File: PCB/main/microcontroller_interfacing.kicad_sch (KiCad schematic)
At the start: 11 parts, among them U1 USB_Micro_B_Female_Connector, U2 CH340G, U3 AT24C256C-SSHL-T, X1 12MHz_SMD_Crystal

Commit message: Update Schematic and BOM
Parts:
- C1, C2: Extended/Basic (none) -> B; JLC Part # (none) -> C1562; Price (none) -> $0.0012
- C4: footprint (none) -> Footprint_EEE3088F:C0402; Extended/Basic (none) -> B; JLC Part # (none) -> C1525; Price (none) -> $0.0011
- D1: Extended/Basic (none) -> B; JLC Part # (none) -> C2286; Price (none) -> $0.0032
- R1: Extended/Basic (none) -> B; JLC Part # (none) -> C23255; Price (none) -> $0.0014
- R5, R6: Extended/Basic (none) -> B; JLC Part # (none) -> C25744; Price (none) -> $0.0007
- U1: Extended/Basic (none) -> E; JLC Part # (none) -> C319160; Populate (none) -> P; Price (none) -> $0.0673
- U2: Extended/Basic (none) -> E; JLC Part # (none) -> C14267; Populate (none) -> P; Price (none) -> $0.5856
- U3: Extended/Basic (none) -> B; JLC Part # (none) -> C6482; Populate (none) -> P; Price (none) -> $1.5556
- X1: Extended/Basic (none) -> B; JLC Part # (none) -> C9002; Populate (none) -> P; Price (none) -> $0.1054
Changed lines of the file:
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@@
+      (effects (font (size 1.27 1.27)) hide)
+    )
+    (property "JLC Part #" "C1562" (id 4) (at 109.22 133.985 0)
+      (effects (font (size 1.27 1.27)) hide)
+    )
+    (property "Price" "$0.0012" (id 5) (at 109.22 133.985 0)
+      (effects (font (size 1.27 1.27)) hide)
+    )
+    (property "Extended/Basic" "B" (id 6) (at 109.22 133.985 0)
       (effects (font (size 1.27 1.27)) hide)
     )
@@
     )
     (property "Datasheet" "" (id 3) (at 71.12 93.98 0)
+      (effects (font (size 1.27 1.27)) hide)
+    )
+    (property "Populate" "P" (id 4) (at 71.12 93.98 0)
+      (effects (font (size 1.27 1.27)) hide)
+    )
+    (property "JLC Part #" "C319160" (id 5) (at 71.12 93.98 0)
+      (effects (font (size 1.27 1.27)) hide)
+    )
+    (property "Price" "$0.0673" (id 6) (at 71.12 93.98 0)
+      (effects (font (size 1.27 1.27)) hide)
+    )
+    (property "Extended/Basic" "E" (id 7) (at 71.12 93.98 0)
       (effects (font (size 1.27 1.27)) hide)
     )
@@
       (effects (font (size 1.27 1.27)) (justify left))
     )
-    (property "Footprint" "" (id 2) (at 207.9752 88.9 0)
+    (property "Footprint" "Footprint_EEE3088F:C0402" (id 2) (at 207.9752 88.9 0)
       (effects (font (size 1.27 1.27)) hide)
     )
@@
       (effects (font (size 1.27 1.27)) hide)
     )
+    (property "JLC Part #" "C1525" (id 4) (at 207.01 85.09 0)
+      (effects (font (size 1.27 1.27)) hide)
+    )
+    (property "Price" "$0.0011" (id 5) (at 207.01 85.09 0)
+      (effects (font (size 1.27 1.27)) hide)
+    )
+    (property "Extended/Basic" "B" (id 6) (at 207.01 85.09 0)
+      (effects (font (size 1.27 1.27)) hide)
+    )
     (pin "1")
     (pin "2")
@@
     )
     (property "Datasheet" "" (id 3) (at 196.85 103.505 0)
+      (effects (font (size 1.27 1.27)) hide)
+    )
+    (property "Populate" "P" (id 4) (at 196.85 103.505 0)
+      (effects (font (size 1.27 1.27)) hide)
+    )
+    (property "JLC Part #" "C6482" (id 5) (at 196.85 103.505 0)
+      (effects (font (size 1.27 1.27)) hide)
+    )
+    (property "Price" "$1.5556" (id 6) (at 196.85 103.505 0)
+      (effects (font (size 1.27 1.27)) hide)
+    )
+    (property "Extended/Basic" "B" (id 7) (at 196.85 103.505 0)
       (effects (font (size 1.27 1.27)) hide)
     )
@@
       (effects (font (size 1.27 1.27)) hide)
     )
+    (property "Populate" "P" (id 4) (at 123.19 131.445 0)
+      (effects (font (size 1.27 1.27)) hide)
+    )
+    (property "JLC Part #" "C9002" (id 5) (at 123.19 131.445 0)
+      (effects (font (size 1.27 1.27)) hide)
+    )
+    (property "Price" "$0.1054" (id 6) (at 123.19 131.445 0)
+      (effects (font (size 1.27 1.27)) hide)
+    )
+    (property "Extended/Basic" "B" (id 7) (at 123.19 131.445 0)
+      (effects (font (size 1.27 1.27)) hide)
+    )
     (pin "1")
     (pin "2")
@@
       (effects (font (size 1.27 1.27)) hide)
     )
+    (property "JLC Part #" "C25744" (id 4) (at 234.95 87.63 0)
+      (effects (font (size 1.27 1.27)) hide)
+    )
+    (property "Price" "$0.0007" (id 5) (at 234.95 87.63 0)
+      (effects (font (size 1.27 1.27)) hide)
+    )
+    (property "Extended/Basic" "B" (id 6) (at 234.95 87.63 0)
+      (effects (font (size 1.27 1.27)) hide)
+    )
     (pin "1")
     (pin "2")
@@
       (effects (font (size 1.27 1.27)) hide)
     )
+    (property "JLC Part #" "C25744" (id 4) (at 222.25 87.63 0)
+      (effects (font (size 1.27 1.27)) hide)
+    )
+    (property "Price" "$0.0007" (id 5) (at 222.25 87.63 0)
+      (effects (font (size 1.27 1.27)) hide)
+    )
+    (property "Extended/Basic" "B" (id 6) (at 222.25 87.63 0)
+      (effects (font (size 1.27 1.27)) hide)
+    )
     (pin "1")
     (pin "2")
@@
     )
     (property "Datasheet" "~" (id 3) (at 91.44 113.03 0)
+      (effects (font (size 1.27 1.27)) hide)
+    )
+    (property "JLC Part #" "C23255" (id 4) (at 91.44 113.03 0)
+      (effects (font (size 1.27 1.27)) hide)
+    )
+    (property "Price" "$0.0014" (id 5) (at 91.44 113.03 0)
+      (effects (font (size 1.27 1.27)) hide)
+    )
+    (property "Extended/Basic" "B" (id 6) (at 91.44 113.03 0)
       (effects (font (size 1.27 1.27)) hide)
     )
@@
       (effects (font (size 1.27 1.27)) hide)
     )
+    (property "JLC Part #" "C1562" (id 4) (at 114.3 149.86 0)
+      (effects (font (size 1.27 1.27)) hide)
+    )
+    (property "Price" "$0.0012" (id 5) (at 114.3 149.86 0)
+      (effects (font (size 1.27 1.27)) hide)
+    )
+    (property "Extended/Basic" "B" (id 6) (at 114.3 149.86 0)
+      (effects (font (size 1.27 1.27)) hide)
+    )
     (pin "1")
     (pin "2")
@@
     )
     (property "Datasheet" "http://www.datasheet5.com/pdf-local-2195953" (id 3) (at 115.57 73.66 0)
+      (effects (font (size 1.27 1.27)) hide)
+    )
+    (property "Populate" "P" (id 4) (at 124.46 93.98 0)
+      (effects (font (size 1.27 1.27)) hide)
+    )
+    (property "JLC Part #" "C14267" (id 5) (at 124.46 93.98 0)
+      (effects (font (size 1.27 1.27)) hide)
+    )
+    (property "Price" "$0.5856" (id 6) (at 124.46 93.98 0)
+      (effects (font (size 1.27 1.27)) hide)
+    )
+    (property "Extended/Basic" "E" (id 7) (at 124.46 93.98 0)
       (effects (font (size 1.27 1.27)) hide)
     )
@@
       (effects (font (size 1.27 1.27)) hide)
     )
+    (property "JLC Part #" "C2286" (id 4) (at 91.44 102.87 0)
+      (effects (font (size 1.27 1.27)) hide)
+    )
+    (property "Price" "$0.0032" (id 5) (at 91.44 102.87 0)
+      (effects (font (size 1.27 1.27)) hide)
+    )
+    (property "Extended/Basic" "B" (id 6) (at 91.44 102.87 0)
+      (effects (font (size 1.27 1.27)) hide)
+    )

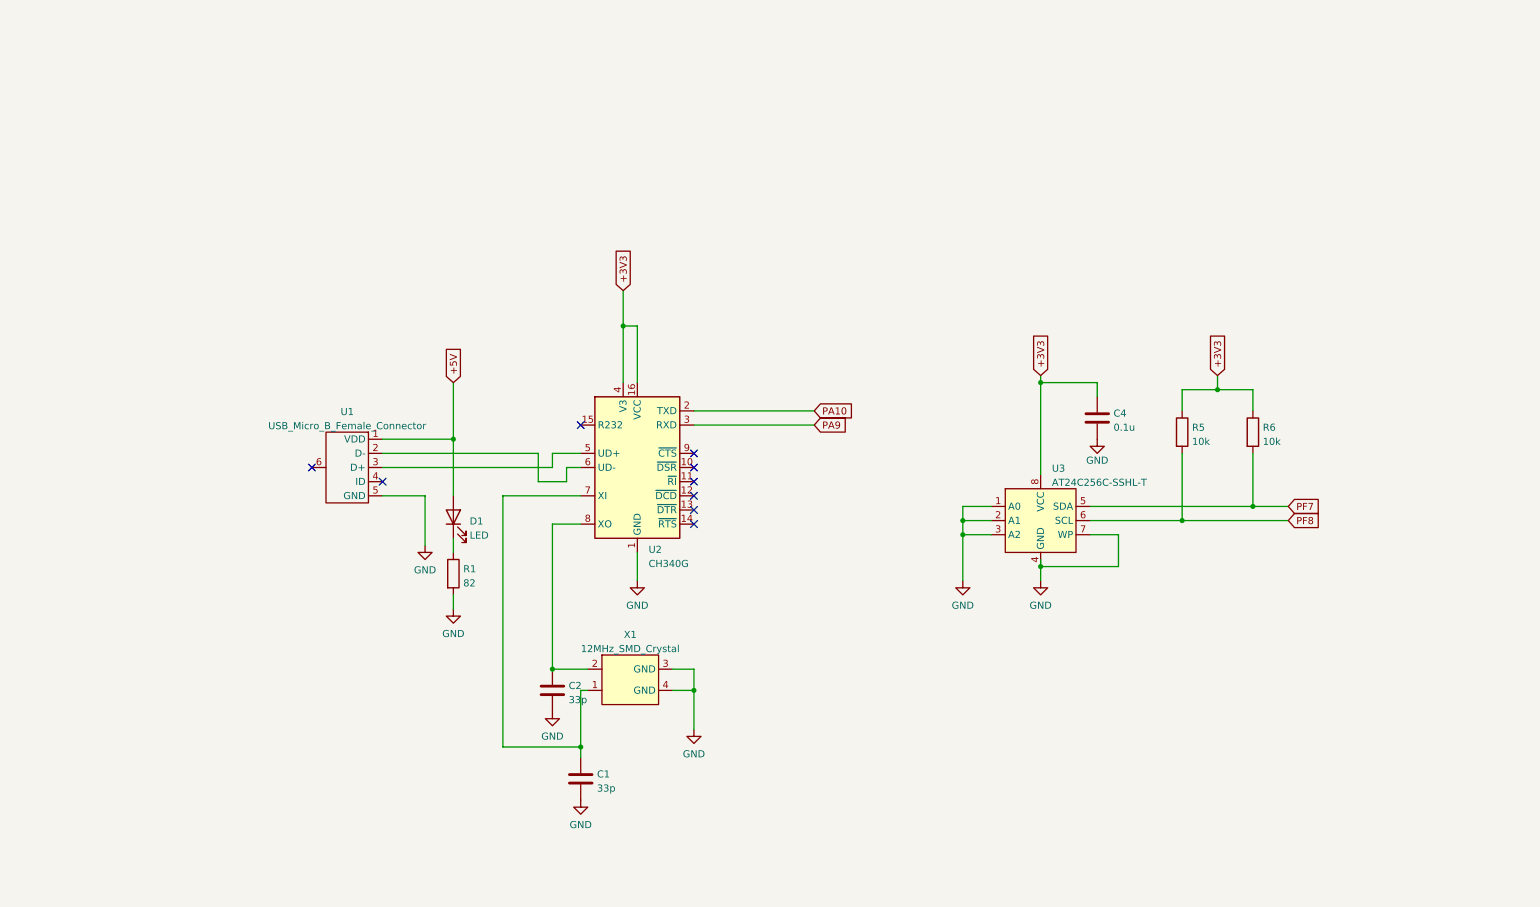
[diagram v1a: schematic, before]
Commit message: Update Schematic with jumpers
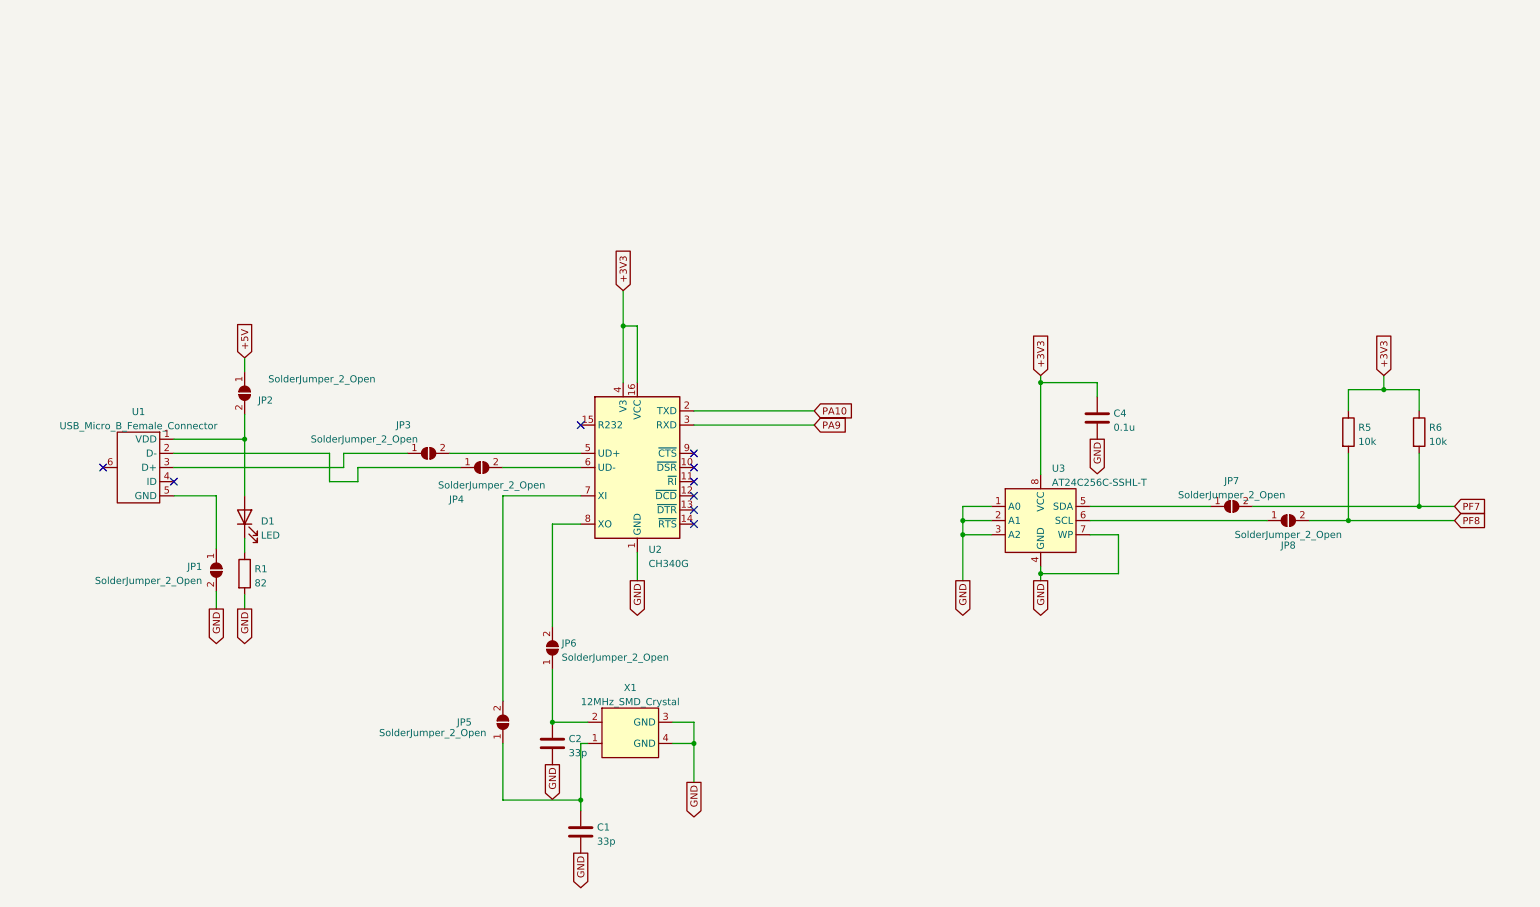
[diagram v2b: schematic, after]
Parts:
- added JP1, JP2, JP3, JP4, JP5, JP6, JP7, JP8: SolderJumper_2_Open, Jumper:SolderJumper-2_P1.3mm_Open_Pad1.0x1.5mm, symbol Jumper:SolderJumper_2_Open
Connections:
- net +5V: now also JP2.1 (A); no longer D1.2 (A), U1.1 (VDD)
- net GND: now also JP1.2 (B); no longer U1.5 (GND)
- net PF7: now also JP7.2 (B); no longer U3.5 (SDA)
- net PF8: now also JP8.2 (B); no longer U3.6 (SCL)
- net at C2.1, X1.2: now also JP6.1 (A); no longer U2.8 (XO)
- net at U1.2 (D-): now also JP4.1 (A); no longer U2.6 (UD-)
- net at U1.3 (D+): now also JP3.1 (A); no longer U2.5 (UD+)
- net at C1.1, X1.1: now also JP5.1 (A); no longer U2.7 (XI)
- new net: D1.2 (A), JP2.2 (B), U1.1 (VDD)
- new net: JP1.1 (A), U1.5 (GND)
- new net: JP6.2 (B), U2.8 (XO)
- new net: JP7.1 (A), U3.5 (SDA)
- new net: JP8.1 (A), U3.6 (SCL)
- new net: JP4.2 (B), U2.6 (UD-)
- new net: JP3.2 (B), U2.5 (UD+)
- new net: JP5.2 (B), U2.7 (XI)
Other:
- moved on the sheet: C1, C2, D1, R1, R5, R6, U1, X1

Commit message: Add notes
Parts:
- U1: value USB_Micro_B_Female_Connector -> USB_Micro_B
- X1: value 12MHz_SMD_Crystal -> 12MHz Crystal
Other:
- company: (none) -> University of Cape Town
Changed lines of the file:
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@@
     (date "2022-03-09")
     (rev "v1.0")
+    (company "University of Cape Town")
+    (comment 1 "Chips used here are EEPROM and FTDI chip (convert between USB connector and UART)")
+    (comment 2 "External Pins connect to STM325f0 Discovery Board")
+    (comment 3 "I2C is being used to connect EEPROM to microcontroller")
+    (comment 4 "Authors: Heather Wimberley")
   )
   (junction (at 182.88 103.505) (diameter 0) (color 0 0 0 0)
@@
     (in_bom yes) (on_board yes) (fields_autoplaced)
     (property "Reference" "U1" (id 0) (at 34.925 83.981 0))
-    (property "Value" "USB_Micro_B_Female_Connector" (id 1) (at 34.925 86.5179 0))
+    (property "Value" "USB_Micro_B" (id 1) (at 34.925 86.5179 0))
     (property "Footprint" "Footprint_EEE3088F:MICRO-USB-SMD_U254-051T-4BH83-S1S" (id 2) (at 33.655 93.98 0)
       (effects (font (size 1.27 1.27)) hide)
@@
     (in_bom yes) (on_board yes) (fields_autoplaced)
     (property "Reference" "X1" (id 0) (at 123.19 133.511 0))
-    (property "Value" "12MHz_SMD_Crystal" (id 1) (at 123.19 136.0479 0))
+    (property "Value" "12MHz Crystal" (id 1) (at 123.19 136.0479 0))
     (property "Footprint" "Footprint_EEE3088F:OSC-SMD_4P-L3.2-W2.5-BL" (id 2) (at 123.19 140.97 0)
       (effects (font (size 1.27 1.27)) hide)

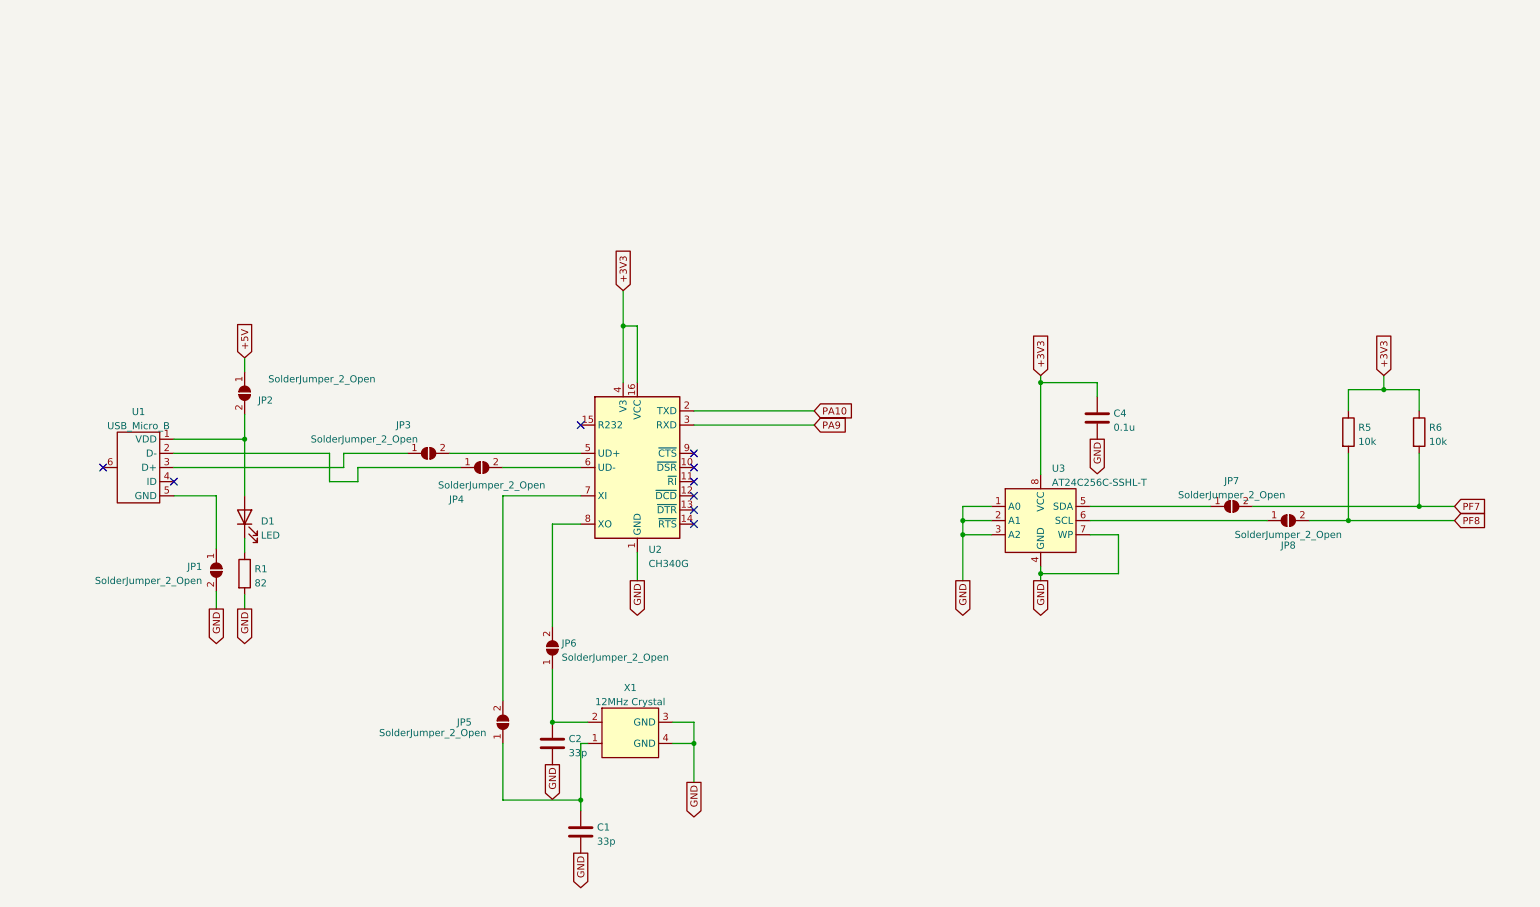
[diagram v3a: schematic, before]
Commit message: Correct jumpers and add headers
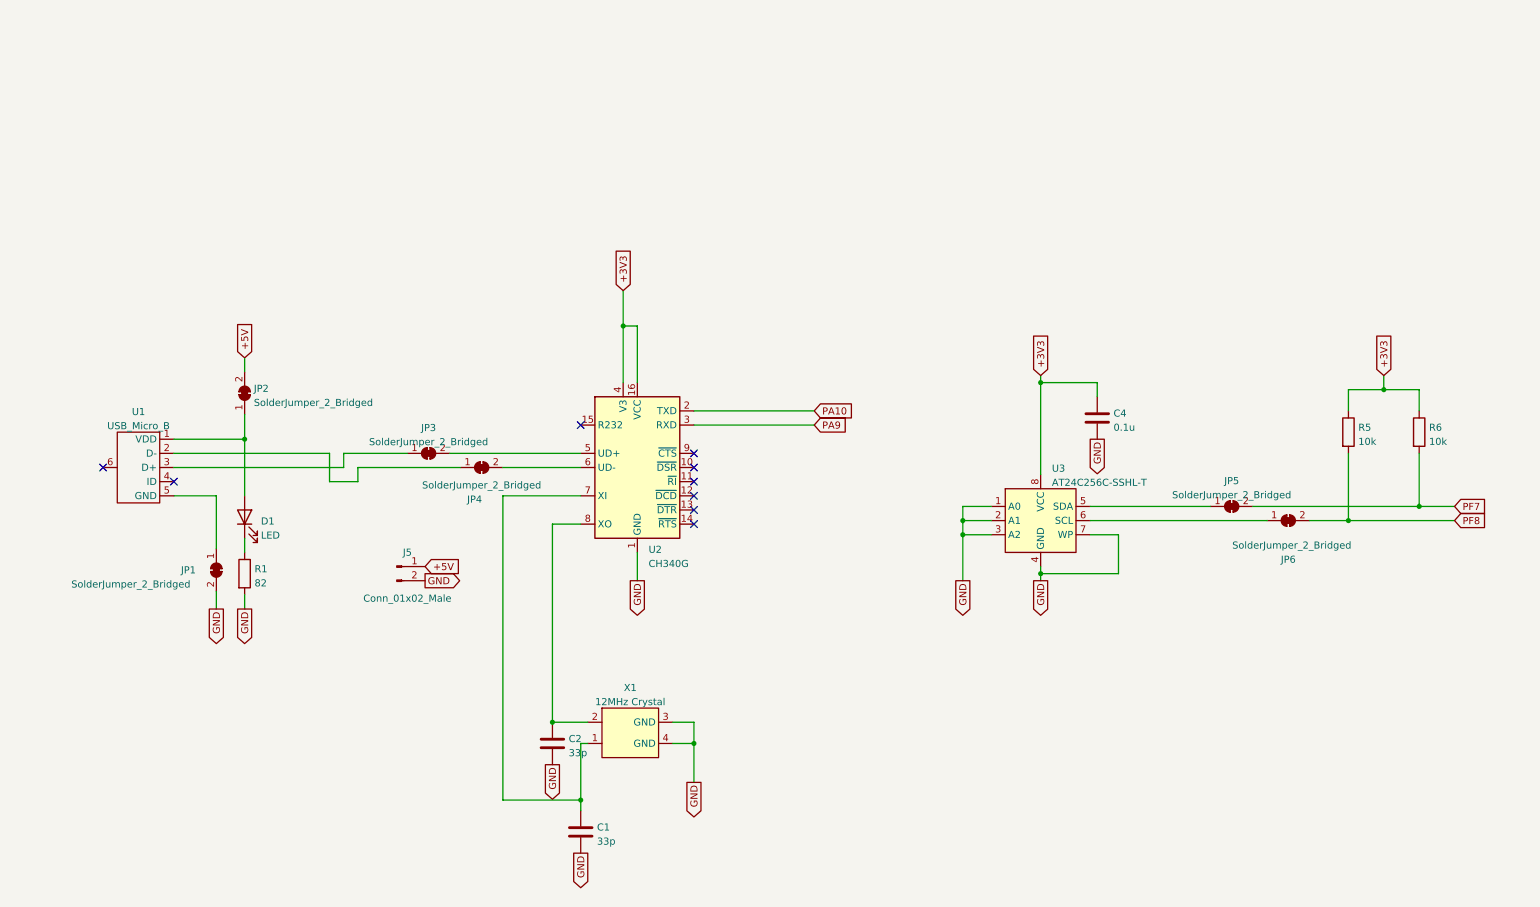
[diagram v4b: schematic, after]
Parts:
- removed JP1, JP2, JP3, JP4, JP5, JP6, JP7, JP8: SolderJumper_2_Open, Jumper:SolderJumper-2_P1.3mm_Open_Pad1.0x1.5mm, symbol Jumper:SolderJumper_2_Open
- added J5: Conn_01x02_Male, symbol Connector:Conn_01x02_Male
- added JP1, JP2, JP3, JP4, JP5, JP6: SolderJumper_2_Bridged, Jumper:SolderJumper-2_P1.3mm_Bridged2Bar_Pad1.0x1.5mm, symbol Jumper:SolderJumper_2_Bridged
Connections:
- net +5V: now also J5.1 (Pin_1), JP2.2 (B)
- net GND: now also J5.2 (Pin_2), JP1.2 (B)
- net PF7: now also JP5.2 (B)
- net PF8: now also JP6.2 (B)
- net at C2.1, X1.2: now also U2.8 (XO)
- net at D1.2 (A), U1.1 (VDD): now also JP2.1 (A)
- net at U1.2 (D-): now also JP4.1 (A)
- net at U1.3 (D+): now also JP3.1 (A)
- net at U1.5 (GND): now also JP1.1 (A)
- net at U3.5 (SDA): now also JP5.1 (A)
- net at U3.6 (SCL): now also JP6.1 (A)
- net at C1.1, X1.1: now also U2.7 (XI)
- net at U2.6 (UD-): now also JP4.2 (B)
- net at U2.5 (UD+): now also JP3.2 (B)

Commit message: Add datasheets and update schematic
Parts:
- J5: footprint (none) -> Connector_PinHeader_1.00mm:PinHeader_1x02_P1.00mm_Vertical
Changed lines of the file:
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@@
     (property "Reference" "J5" (id 0) (at 83.185 109.22 0))
     (property "Value" "Conn_01x02_Male" (id 1) (at 83.185 117.475 0))
-    (property "Footprint" "" (id 2) (at 81.28 111.76 0)
+    (property "Footprint" "Connector_PinHeader_1.00mm:PinHeader_1x02_P1.00mm_Vertical" (id 2) (at 81.28 111.76 0)
       (effects (font (size 1.27 1.27)) hide)
     )
